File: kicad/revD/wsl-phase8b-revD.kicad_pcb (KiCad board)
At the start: 4 copper layers, 250 x 240 mm, 299 parts, among them J1 J_PI, J10 J_MOTION_M 5.08mm, J11 J_MOTION_M2 5.08mm, J12 J_MOTION_M1 5.08mm, J13 J_LAMP_LED, J14 J_SAFETY, J15 J_SLOW_IN_C, J16 J_EXT_I2C, J2 J_PWR 5V, J3 J_FAST_IN, J4 J_SLOW_IN_A, J5 J_SLOW_IN_B, J6 J_MOTION_S 5.08mm, J7 J_MOTION_T 5.08mm, J8 J_MOTION_SP 5.08mm, J9 J_MOTION_BE 5.08mm, K1 G5LE S, K2 G5LE T, K3 G5LE SP, K4 G5LE BE, K5 G5LE M, K6 G5LE M2, K7 G5LE M1 DNP, Q1 MMBT3904 S, Q10 2N7002 LED L_STRIKE, Q11 2N7002 LED L_FOUL, Q12 AO3400A kick, Q13 AO3400A wdog, Q14 AO3401A rail pass, Q15 MMBT3904 AND ARM, Q16 MMBT3904 AND RP_OK, Q17 2N7002LT1G TAP 555, Q18 2N7002LT1G TAP KICK, Q19 2N7002LT1G TAP ARM, Q2 MMBT3904 T, Q20 2N7002LT1G TAP RPOK, Q3 MMBT3904 SP, Q4 MMBT3904 BE, Q5 MMBT3904 M, Q6 MMBT3904 M2, Q7 MMBT3904 M1, Q8 2N7002 LED L_FIRST, Q9 2N7002 LED L_SECOND, U1 MCP23017 MCP_IN_A, U10 PC817 DIELL_L, U11 PC817 DIELL_R, U12 PC817 GS1, U13 PC817 GS2, U14 PC817 GS3, U15 PC817 GS4, U16 PC817 GS5, U17 PC817 GS6, U18 PC817 GS7, U19 PC817 GS8, U2 MCP23017 MCP_IN_B, U20 PC817 GS9, U21 PC817 GS10, U22 PC817 GP, U23 PC817 OS, U24 PC817 BS, U25 PC817 PBZ, U26 PC817 PBC, U27 PC817 FOUL, U28 PC817 TENTH, U29 PC817 MAN_T, U3 MCP23017 MCP_OUT_A, U30 PC817 MAN_S, U31 PC817 MAN_SWS, U32 PC817 MAN_SWSR, U33 PC817 AUX1, U34 PC817 AUX2, U35 PC817 AUX3, U36 PC817 AUX4, U37 PC817 AUX5, U38 PC817 AUX6, U39 PC817 AUX7, U4 PC817 SA, U40 PC817 AUX8, U41 PC817 AUX9, U42 PC817 AUX10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

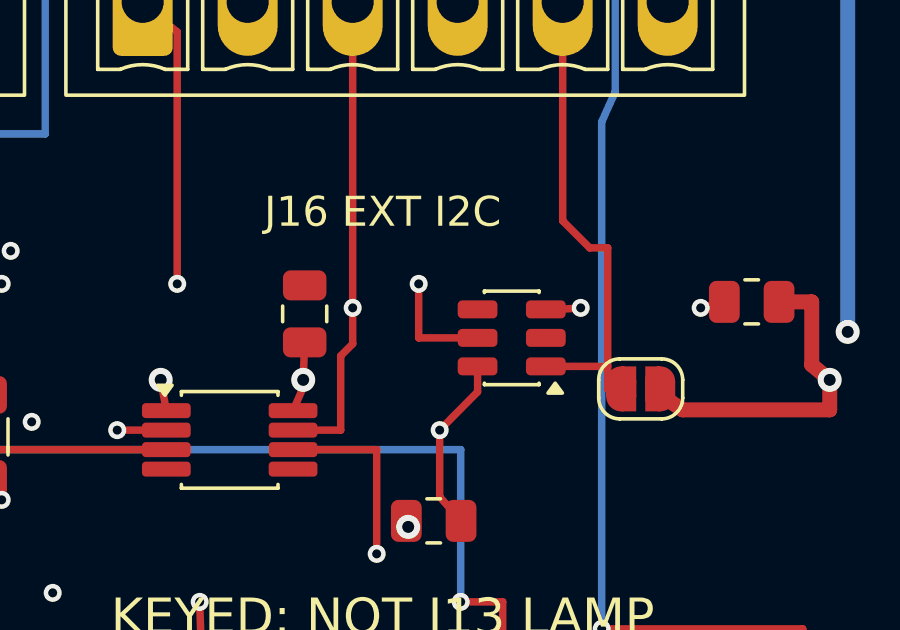
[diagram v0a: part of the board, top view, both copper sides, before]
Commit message: Round-3 fix batch: Codex re-review of the round-2 package — 8 findings, all fixed; full gate chain re-proven
Finding 1 (CRITICAL, fw): v1.2.2 boot-order regression — tap_assert_input_only()
ran before init_inputs(), so every boot latched a spurious tap_dir/SA fault
(GP6-13 still at reset FUNCSEL) and refused RP_OK. Fixed with an inputs_inited
gate (rev_id_inited pattern) + a second invariant pass right after init_inputs().
New test_v12 section R replicates main()'s LITERAL boot order on reset-state pins.

Finding 2 (MAJOR, board): unfused rail sneak path — SRV05-4 VP rode the FUSED
J16_5V node; with JP1 bridged, a J16 5V-to-GND short pulled continuous VCC_3V3
current through IO1's pulse-rated steering diode, defeating the polyfuse. VP now
rides VCC_5V UPSTREAM of F1; the fused pin keeps ESD via the ex-spare IO3
channel (U47.4). Generator/router/audits updated; 271/223 unchanged;
Safety_Rail 13; router self-check 0 (2167 actions); DRC 0/0/0
(DRC-revD-round3-r1.rpt, first pass); board audit ALL PASS (new fail-closed
U47.5-on-VCC_5V assert); diff vs rev-C CLEAN; isolation minima unchanged
2.650/3.350. WVR-ERC-1 waiver now matches the GND/AGND pin pair
order-insensitively (GND pin-order flip from U47.4 leaving GND) — stricter:
both pins must be named.

Finding 3 (MAJOR, Pi): fw_identity chain dead-ended — the typed record was
drained and discarded, and nothing ever sent ID. rp2040_link.start() now sends
ID (request_identity()); _consume_link_records gained the fw_identity branch:
fi1_image and pcb_rev_mismatch are FAULT severity (declared revC expects
strap-read "unknown"). +4 daemon tests, +2 link tests.

Finding 4 (minor, docs): FI-1 BOOTSEL gate vs the bootrom — a plain power cycle
with the jumper held enters the ROM bootloader and can never satisfy the gate.
Working sequences (hold-through-flash / jumper + picotool reboot) documented in
README.md and first-article FA-7 step 0.

Finding 5 (minor, fw): 16-bit epoch aliasing — after 65536 ring-adopting
reboots a stale 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
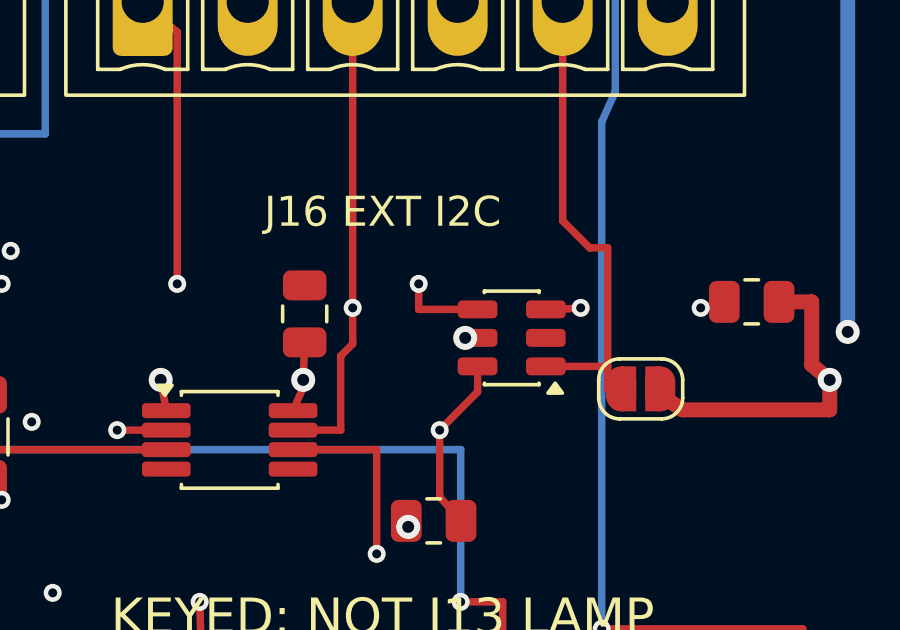
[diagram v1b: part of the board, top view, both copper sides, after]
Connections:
- U47 pad 4: GND -> J16_5V
- U47 pad 5: J16_5V -> VCC_5V
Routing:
- net J16_5V: track 35.8 -> 34.8 mm
- net VCC_5V: track 534.5 -> 535.1 mm, vias 18 -> 19

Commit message: Round-4 board (Codex 'Rev-D r5' + Claude F4 fix): 47k PC817 collector pull-ups, fab r4 tombstoned, r5 release package
Coordinated value-only change: SKiDL generator Rpu_* 10k -> 47k with rationale,
netlist + kicad_pcb exactly 40 Value-field swaps, ZERO copper/geometry/net changes
(frozen-copper rule respected). Fab r4 captured the 47k change but predates the
runtime-bias gate -> tombstoned; r5 is the orderable package (manifest 45/45,
DRC 0/0/0 in reports/).

Claude audit 2026-07-24: full gate chain independently re-run - generator ERC
waiver PASS, netlist reproduced BYTE-IDENTICAL 1d5d36f2..., revC->revD diff clean
55/39/11, kicad-cli 10.0 DRC 0/0, audit_revD_board ALL PASS (exact R4..R82 47k
set), netclass 103/4/13/82/21 Safety_Rail=13, r5 manifest re-hash 45/45,
first-article map 271 rows/40x47k/28 DNP. F4 fixed: ERC canonicalizer now orders
operands inside conflict lines so regeneration reproduces ERC c5dfdf52...
byte-identically. Electrical merit verified (opto sink 264uA->56uA, VIH margin
0.613V); turn-off edge + transient-immunity risks measurement-gated by revised
FA-9 (both edges <=100us, hot open-node >=2.84V) with fleet NO-GO retained.

Co-Authored-By: Claude Fable 5 <noreply@anthropic.com>
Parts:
- R10, R12, R14, R16, R18, R20, R22, R24, R26, R28, R30, R32, R34, R36, R38, R4, R40, R42, R44, R46, R48, R50, R52, R54, R56, R58, R6, R60, R62, R64, R66, R68, R70, R72, R74, R76, R78, R8, R80, R82: value 10k -> 47k
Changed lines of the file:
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@@
 			)
 		)
-		(property "Value" "10k"
+		(property "Value" "47k"
 			(at 0 1.65 0)
 			(layer "F.Fab")
@@
 			)
 		)
-		(property "Value" "10k"
+		(property "Value" "47k"
 			(at 0 1.65 0)
 			(layer "F.Fab")
@@
 			)
 		)
-		(property "Value" "10k"
+		(property "Value" "47k"
 			(at 0 1.65 0)
 			(layer "F.Fab")
@@
 			)
 		)
-		(property "Value" "10k"
+		(property "Value" "47k"
 			(at 0 1.65 0)
 			(layer "F.Fab")
@@
 			)
 		)
-		(property "Value" "10k"
+		(property "Value" "47k"
 			(at 0 1.65 0)
 			(layer "F.Fab")
@@
 			)
 		)
-		(property "Value" "10k"
+		(property "Value" "47k"
 			(at 0 1.65 0)
 			(layer "F.Fab")
@@
 			)
 		)
-		(property "Value" "10k"
+		(property "Value" "47k"
 			(at 0 1.65 0)
 			(layer "F.Fab")
@@
 			)
 		)
-		(property "Value" "10k"
+		(property "Value" "47k"
 			(at 0 1.65 0)
 			(layer "F.Fab")
@@
 			)
 		)
-		(property "Value" "10k"
+		(property "Value" "47k"
 			(at 0 1.65 0)
 			(layer "F.Fab")
@@
 			)
 		)
-		(property "Value" "10k"
+		(property "Value" "47k"
 			(at 0 1.65 0)
 			(layer "F.Fab")
@@
 			)
 		)
-		(property "Value" "10k"
+		(property "Value" "47k"
 			(at 0 1.65 0)
 			(layer "F.Fab")
@@
 			)
 		)
-		(property "Value" "10k"
+		(property "Value" "47k"
 			(at 0 1.65 0)
 			(layer "F.Fab")
@@
 			)
 		)
-		(property "Value" "10k"
+		(property "Value" "47k"
 			(at 0 1.65 0)
 			(layer "F.Fab")
@@
 			)
 		)
-		(property "Value" "10k"
+		(property "Value" "47k"
 			(at 0 1.65 0)
 			(layer "F.Fab")
@@
 			)
 		)
-		(property "Value" "10k"
+		(property "Value" "47k"
 			(at 0 1.65 0)
 			(layer "F.Fab")
@@
 			)
 		)
-		(property "Value" "10k"
+		(property "Value" "47k"
 			(at 0 1.65 0)
 			(layer "F.Fab")
@@
 			)
 		)
-		(property "Value" "10k"
+		(property "Value" "47k"
 			(at 0 1.65 0)
 			(layer "F.Fab")
@@
 			)
 		)
-		(property "Value" "10k"
+		(property "Value" "47k"
 			(at 0 1.65 0)
 			(layer "F.Fab")
@@
 			)
 		)
-		(property "Value" "10k"
+		(property "Value" "47k"
 			(at 0 1.65 0)
 			(layer "F.Fab")
@@
 			)
 		)
-		(property "Value" "10k"
+		(property "Value" "47k"
 			(at 0 1.65 0)
 			(layer "F.Fab")
@@
 			)
 		)
-		(property "Value" "10k"
+		(property "Value" "47k"
 			(at 0 1.65 0)
 			(layer "F.Fab")
@@
 			)
 		)
-		(property "Value" "10k"
+		(property "Value" "47k"
 			(at 0 1.65 0)
 			(layer "F.Fab")
@@
 			)
 		)
-		(property "Value" "10k"
+		(property "Value" "47k"
 			(at 0 1.65 0)
 			(layer "F.Fab")
@@
 			)
 		)
-		(property "Value" "10k"
+		(property "Value" "47k"
 			(at 0 1.65 0)
 			(layer "F.Fab")
@@
 			)
 		)
-		(property "Value" "10k"
+		(property "Value" "47k"
 			(at 0 1.65 0)
 			(layer "F.Fab")
@@
 			)
 		)
-		(property "Value" "10k"
+		(property "Value" "47k"
 			(at 0 1.65 0)
 			(layer "F.Fab")
@@
 			)
 		)
-		(property "Value" "10k"
+		(property "Value" "47k"
 			(at 0 1.65 0)
 			(layer "F.Fab")
@@
 			)
 		)
-		(property "Value" "10k"
+		(property "Value" "47k"
 			(at 0 1.65 0)
 			(layer "F.Fab")
@@
 			)
 		)
-		(property "Value" "10k"
+		(property "Value" "47k"
 			(at 0 1.65 0)
 			(layer "F.Fab")
@@
 			)
 		)
-		(property "Value" "10k"
+		(property "Value" "47k"
 			(at 0 1.65 0)
 			(layer "F.Fab")
@@
 			)
 		)
-		(property "Value" "10k"
+		(property "Value" "47k"
 			(at 0 1.65 0)
 			(layer "F.Fab")
@@
 			)
 		)
-		(property "Value" "10k"
+		(property "Value" "47k"
 			(at 0 1.65 0)
 			(layer "F.Fab")
@@
 			)
 		)
-		(property "Value" "10k"
+		(property "Value" "47k"
 			(at 0 1.65 0)
 			(layer "F.Fab")
@@
 			)
 		)
-		(property "Value" "10k"
+		(property "Value" "47k"
 			(at 0 1.65 0)
 			(layer "F.Fab")
@@
 			)
 		)
-		(property "Value" "10k"
+		(property "Value" "47k"
 			(at 0 1.65 0)
 			(layer "F.Fab")
@@
 			)
 		)
-		(property "Value" "10k"
+		(property "Value" "47k"
 			(at 0 1.65 0)
 			(layer "F.Fab")
@@
 			)
 		)
-		(property "Value" "10k"
+		(property "Value" "47k"
 			(at 0 1.65 0)
 			(layer "F.Fab")
@@
 			)
 		)
-		(property "Value" "10k"
+		(property "Value" "47k"
 			(at 0 1.65 0)
 			(layer "F.Fab")
@@
 			)
 		)
-		(property "Value" "10k"
+		(property "Value" "47k"
 			(at 0 1.65 0)
 			(layer "F.Fab")
@@
 			)
 		)
-		(property "Value" "10k"
+		(property "Value" "47k"
 			(at 0 1.65 0)
 			(layer "F.Fab")

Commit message: rev-D r6: per-channel input protection on all 40 opto channels + review batch
Dylan reopened copper 2026-07-25 so the first article is fleet-intent rather
than frozen-and-bodged. Board revision stays D (never fabricated); this is fab
iteration r6. Firmware NOT touched, NOT flashed.

COPPER (all 40 channels, uniform - no per-channel stuffing decision):
  FIELD_WET_V -[Rin 2k2]- FIELD_RIN_<n> -[Dser 1N4148WS]- FIELD_LED_<n>
  -[PC817 LED]- FIELD_<n>, with Dclamp_<n> (1N4148WS) anti-parallel across the
  LED and Cflt_<n> (0805, DNP) on the logic side.
  Dser_*/Dclamp_* = D18-D97, POPULATED. Cflt_* = C17-C56, DNP.

Only series-block + clamp TOGETHER close the case: a clamp alone backfeeds Rin
into the shared FIELD_WET_V rail (Vw pulled to 10.8 V at 9.79 mA on PBZ); a
series diode alone leaves LED reverse set by a leakage divider rather than by
construction. The series position is never DNP-empty - that would open-circuit
the channel.

Counts: parts 271->391, nets 223->263, Field_Sense 82->122, DNP 28->68,
placed 243->323, JLC-placed 226->306. Safety_Rail EXACTLY 13 - unchanged.
EXPECTED_JLC_LINES stays 27: the 80 diodes join the existing 1N4148WS line
(qty 8 -> 88), so zero new JLC-assembled part classes.

FR reviews (P1 scripture, in the run log): FR-16 1N4148WS/SOD-323 PASS with an
explicit polarity proof (symbol pin 1 = K, F.Fab cathode bar toward pad 1,
package band at cathode - three independent confirmations); FR-17 2.2uF X7R
0805 PASS (DNP); FR-18 10nF X7R 0805 PASS (DNP, already a locked part).

REVIEW BATCH - 15 findings verified, 14 real and fixed, 1 rejected:
- Spec D.5 claimed a 1.06 mm / 1.77x clearance minimum. Bracketed with
  kicad-cli: 0.90 -> 0 violations, 0.95 -> 117 ("actual 0.9100 mm"), 1.00 -> 148.
  TRUE MINIMUM 0.910 mm = 1.52x, and the binding pair is an r6 clamp pad vs the
  next row's FIELD_LED track, not the track-to-track pair analysed. Gate still
  0/0/0. Corrected in the spec and the .kicad_dru.
- Spec J5/I.2 demanded "sole CHANGED_PART = 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
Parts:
- added C17: 10nF X7R DNP, Capacitor_SMD:C_0805_2012Metric, F.Cu at (86.0, 17.6)
- added C18: 10nF X7R DNP, Capacitor_SMD:C_0805_2012Metric, F.Cu at (86.0, 23.3)
- added C19: 10nF X7R DNP, Capacitor_SMD:C_0805_2012Metric, F.Cu at (86.0, 29.0)
- added C20: 10nF X7R DNP, Capacitor_SMD:C_0805_2012Metric, F.Cu at (86.0, 34.7)
- added C21: 10nF X7R DNP, Capacitor_SMD:C_0805_2012Metric, F.Cu at (86.0, 40.4)
- added C22: 10nF X7R DNP, Capacitor_SMD:C_0805_2012Metric, F.Cu at (86.0, 46.1)
- added C23: 10nF X7R DNP, Capacitor_SMD:C_0805_2012Metric, F.Cu at (86.0, 51.8)
- added C24: 10nF X7R DNP, Capacitor_SMD:C_0805_2012Metric, F.Cu at (86.0, 57.5)
- added C25: 2.2uF X7R DNP, Capacitor_SMD:C_0805_2012Metric, F.Cu at (86.0, 63.2)
- added C26: 2.2uF X7R DNP, Capacitor_SMD:C_0805_2012Metric, F.Cu at (86.0, 68.9)
- added C27: 2.2uF X7R DNP, Capacitor_SMD:C_0805_2012Metric, F.Cu at (86.0, 74.6)
- added C28: 2.2uF X7R DNP, Capacitor_SMD:C_0805_2012Metric, F.Cu at (86.0, 80.3)
- added C29: 2.2uF X7R DNP, Capacitor_SMD:C_0805_2012Metric, F.Cu at (86.0, 86.0)
- added C30: 2.2uF X7R DNP, Capacitor_SMD:C_0805_2012Metric, F.Cu at (86.0, 91.7)
- added C31: 2.2uF X7R DNP, Capacitor_SMD:C_0805_2012Metric, F.Cu at (86.0, 97.4)
- added C32: 2.2uF X7R DNP, Capacitor_SMD:C_0805_2012Metric, F.Cu at (86.0, 103.1)
- added C33: 2.2uF X7R DNP, Capacitor_SMD:C_0805_2012Metric, F.Cu at (86.0, 108.8)
- added C34: 2.2uF X7R DNP, Capacitor_SMD:C_0805_2012Metric, F.Cu at (86.0, 114.5)
- added C35: 2.2uF X7R DNP, Capacitor_SMD:C_0805_2012Metric, F.Cu at (86.0, 120.2)
- added C36: 2.2uF X7R DNP, Capacitor_SMD:C_0805_2012Metric, F.Cu at (86.0, 125.9)
- added C37: 2.2uF X7R DNP, Capacitor_SMD:C_0805_2012Metric, F.Cu at (86.0, 131.6)
- added C38: 2.2uF X7R DNP, Capacitor_SMD:C_0805_2012Metric, F.Cu at (86.0, 137.3)
- added C39: 2.2uF X7R DNP, Capacitor_SMD:C_0805_2012Metric, F.Cu at (86.0, 143.0)
- added C40: 2.2uF X7R DNP, Capacitor_SMD:C_0805_2012Metric, F.Cu at (86.0, 148.7)
- added C41: 2.2uF X7R DNP, Capacitor_SMD:C_0805_2012Metric, F.Cu at (86.0, 154.4)
- added C42: 2.2uF X7R DNP, Capacitor_SMD:C_0805_2012Metric, F.Cu at (86.0, 160.1)
- added C43: 2.2uF X7R DNP, Capacitor_SMD:C_0805_2012Metric, F.Cu at (86.0, 165.8)
- added C44: 2.2uF X7R DNP, Capacitor_SMD:C_0805_2012Metric, F.Cu at (86.0, 171.5)
- added C45: 2.2uF X7R DNP, Capacitor_SMD:C_0805_2012Metric, F.Cu at (86.0, 177.2)
- added C46: 2.2uF X7R DNP, Capacitor_SMD:C_0805_2012Metric, F.Cu at (86.0, 182.9)
- added C47: 2.2uF X7R DNP, Capacitor_SMD:C_0805_2012Metric, F.Cu at (86.0, 188.6)
- added C48: 2.2uF X7R DNP, Capacitor_SMD:C_0805_2012Metric, F.Cu at (86.0, 194.3)
- added C49: 2.2uF X7R DNP, Capacitor_SMD:C_0805_2012Metric, F.Cu at (86.0, 200.0)
- added C50: 2.2uF X7R DNP, Capacitor_SMD:C_0805_2012Metric, F.Cu at (86.0, 205.7)
- added C51: 2.2uF X7R DNP, Capacitor_SMD:C_0805_2012Metric, F.Cu at (86.0, 211.4)
- added C52: 2.2uF X7R DNP, Capacitor_SMD:C_0805_2012Metric, F.Cu at (86.0, 217.1)
- added C53: 2.2uF X7R DNP, Capacitor_SMD:C_0805_2012Metric, F.Cu at (86.0, 222.8)
- added C54: 2.2uF X7R DNP, Capacitor_SMD:C_0805_2012Metric, F.Cu at (86.0, 228.5)
- added C55: 2.2uF X7R DNP, Capacitor_SMD:C_0805_2012Metric, F.Cu at (86.0, 234.2)
- added C56: 2.2uF X7R DNP, Capacitor_SMD:C_0805_2012Metric, F.Cu at (90.0, 237.1)
- added D18: 1N4148, Diode_SMD:D_SOD-323, F.Cu at (62.0, 11.2)
- added D19: 1N4148, Diode_SMD:D_SOD-323, F.Cu at (70.0, 14.5)
- added D20: 1N4148, Diode_SMD:D_SOD-323, F.Cu at (62.0, 19.9)
- added D21: 1N4148, Diode_SMD:D_SOD-323, F.Cu at (70.0, 20.2)
- added D22: 1N4148, Diode_SMD:D_SOD-323, F.Cu at (62.0, 22.6)
- added D23: 1N4148, Diode_SMD:D_SOD-323, F.Cu at (70.0, 25.9)
- added D24: 1N4148, Diode_SMD:D_SOD-323, F.Cu at (62.0, 28.3)
- added D25: 1N4148, Diode_SMD:D_SOD-323, F.Cu at (70.0, 31.6)
- added D26: 1N4148, Diode_SMD:D_SOD-323, F.Cu at (62.0, 34.0)
- added D27: 1N4148, Diode_SMD:D_SOD-323, F.Cu at (70.0, 37.3)
- added D28: 1N4148, Diode_SMD:D_SOD-323, F.Cu at (62.0, 39.7)
- added D29: 1N4148, Diode_SMD:D_SOD-323, F.Cu at (70.0, 43.0)
- added D30: 1N4148, Diode_SMD:D_SOD-323, F.Cu at (62.0, 45.4)
- added D31: 1N4148, Diode_SMD:D_SOD-323, F.Cu at (70.0, 48.7)
- added D32: 1N4148, Diode_SMD:D_SOD-323, F.Cu at (62.0, 51.1)
- added D33: 1N4148, Diode_SMD:D_SOD-323, F.Cu at (70.0, 54.4)
- added D34: 1N4148, Diode_SMD:D_SOD-323, F.Cu at (62.0, 56.8)
- added D35: 1N4148, Diode_SMD:D_SOD-323, F.Cu at (70.0, 60.1)
- added D36: 1N4148, Diode_SMD:D_SOD-323, F.Cu at (62.0, 62.5)
- added D37: 1N4148, Diode_SMD:D_SOD-323, F.Cu at (70.0, 65.8)
- added D38: 1N4148, Diode_SMD:D_SOD-323, F.Cu at (62.0, 68.2)
- added D39: 1N4148, Diode_SMD:D_SOD-323, F.Cu at (70.0, 71.5)
- added D40: 1N4148, Diode_SMD:D_SOD-323, F.Cu at (62.0, 73.9)
- added D41: 1N4148, Diode_SMD:D_SOD-323, F.Cu at (70.0, 77.2)
- added D42: 1N4148, Diode_SMD:D_SOD-323, F.Cu at (62.0, 79.6)
- added D43: 1N4148, Diode_SMD:D_SOD-323, F.Cu at (70.0, 82.9)
- added D44: 1N4148, Diode_SMD:D_SOD-323, F.Cu at (62.0, 85.3)
- added D45: 1N4148, Diode_SMD:D_SOD-323, F.Cu at (70.0, 88.6)
- added D46: 1N4148, Diode_SMD:D_SOD-323, F.Cu at (62.0, 91.0)
- added D47: 1N4148, Diode_SMD:D_SOD-323, F.Cu at (70.0, 94.3)
- added D48: 1N4148, Diode_SMD:D_SOD-323, F.Cu at (62.0, 96.7)
- added D49: 1N4148, Diode_SMD:D_SOD-323, F.Cu at (70.0, 100.0)
- added D50: 1N4148, Diode_SMD:D_SOD-323, F.Cu at (62.0, 102.4)
- added D51: 1N4148, Diode_SMD:D_SOD-323, F.Cu at (70.0, 105.7)
- added D52: 1N4148, Diode_SMD:D_SOD-323, F.Cu at (62.0, 108.1)
- added D53: 1N4148, Diode_SMD:D_SOD-323, F.Cu at (70.0, 111.4)
- added D54: 1N4148, Diode_SMD:D_SOD-323, F.Cu at (62.0, 113.8)
- added D55: 1N4148, Diode_SMD:D_SOD-323, F.Cu at (70.0, 117.1)
- added D56: 1N4148, Diode_SMD:D_SOD-323, F.Cu at (62.0, 119.5)
- added D57: 1N4148, Diode_SMD:D_SOD-323, F.Cu at (70.0, 122.8)
- added D58: 1N4148, Diode_SMD:D_SOD-323, F.Cu at (62.0, 125.2)
- added D59: 1N4148, Diode_SMD:D_SOD-323, F.Cu at (70.0, 128.5)
- added D60: 1N4148, Diode_SMD:D_SOD-323, F.Cu at (62.0, 130.9)
- added D61: 1N4148, Diode_SMD:D_SOD-323, F.Cu at (70.0, 134.2)
- added D62: 1N4148, Diode_SMD:D_SOD-323, F.Cu at (62.0, 136.6)
- added D63: 1N4148, Diode_SMD:D_SOD-323, F.Cu at (70.0, 139.9)
- added D64: 1N4148, Diode_SMD:D_SOD-323, F.Cu at (62.0, 142.3)
- added D65: 1N4148, Diode_SMD:D_SOD-323, F.Cu at (70.0, 145.6)
- added D66: 1N4148, Diode_SMD:D_SOD-323, F.Cu at (62.0, 148.0)
- added D67: 1N4148, Diode_SMD:D_SOD-323, F.Cu at (70.0, 151.3)
- added D68: 1N4148, Diode_SMD:D_SOD-323, F.Cu at (62.0, 153.7)
- added D69: 1N4148, Diode_SMD:D_SOD-323, F.Cu at (70.0, 157.0)
- added D70: 1N4148, Diode_SMD:D_SOD-323, F.Cu at (62.0, 159.4)
- added D71: 1N4148, Diode_SMD:D_SOD-323, F.Cu at (70.0, 162.7)
- added D72: 1N4148, Diode_SMD:D_SOD-323, F.Cu at (62.0, 165.1)
- added D73: 1N4148, Diode_SMD:D_SOD-323, F.Cu at (70.0, 168.4)
- added D74: 1N4148, Diode_SMD:D_SOD-323, F.Cu at (62.0, 170.8)
- added D75: 1N4148, Diode_SMD:D_SOD-323, F.Cu at (70.0, 174.1)
- added D76: 1N4148, Diode_SMD:D_SOD-323, F.Cu at (62.0, 176.5)
- added D77: 1N4148, Diode_SMD:D_SOD-323, F.Cu at (70.0, 179.8)
- added D78: 1N4148, Diode_SMD:D_SOD-323, F.Cu at (62.0, 182.2)
- added D79: 1N4148, Diode_SMD:D_SOD-323, F.Cu at (70.0, 185.5)
- added D80: 1N4148, Diode_SMD:D_SOD-323, F.Cu at (62.0, 187.9)
- added D81: 1N4148, Diode_SMD:D_SOD-323, F.Cu at (70.0, 191.2)
- added D82: 1N4148, Diode_SMD:D_SOD-323, F.Cu at (62.0, 193.6)
- added D83: 1N4148, Diode_SMD:D_SOD-323, F.Cu at (70.0, 196.9)
- added D84: 1N4148, Diode_SMD:D_SOD-323, F.Cu at (62.0, 199.3)
- added D85: 1N4148, Diode_SMD:D_SOD-323, F.Cu at (70.0, 202.6)
- added D86: 1N4148, Diode_SMD:D_SOD-323, F.Cu at (62.0, 205.0)
- added D87: 1N4148, Diode_SMD:D_SOD-323, F.Cu at (70.0, 208.3)
- added D88: 1N4148, Diode_SMD:D_SOD-323, F.Cu at (62.0, 210.7)
- added D89: 1N4148, Diode_SMD:D_SOD-323, F.Cu at (70.0, 214.0)
- added D90: 1N4148, Diode_SMD:D_SOD-323, F.Cu at (62.0, 216.4)
- added D91: 1N4148, Diode_SMD:D_SOD-323, F.Cu at (70.0, 219.7)
- added D92: 1N4148, Diode_SMD:D_SOD-323, F.Cu at (62.0, 222.1)
- added D93: 1N4148, Diode_SMD:D_SOD-323, F.Cu at (70.0, 225.4)
- added D94: 1N4148, Diode_SMD:D_SOD-323, F.Cu at (62.0, 227.8)
- added D95: 1N4148, Diode_SMD:D_SOD-323, F.Cu at (70.0, 231.1)
- added D96: 1N4148, Diode_SMD:D_SOD-323, F.Cu at (62.0, 233.5)
- added D97: 1N4148, Diode_SMD:D_SOD-323, F.Cu at (70.0, 236.8)
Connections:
- R11 pad 2: FIELD_LED_TA2 -> FIELD_RIN_TA2
- R13 pad 2: FIELD_LED_TB -> FIELD_RIN_TB
- R15 pad 2: FIELD_LED_DIELL_L -> FIELD_RIN_DIELL_L
- R17 pad 2: FIELD_LED_DIELL_R -> FIELD_RIN_DIELL_R
- R19 pad 2: FIELD_LED_GS1 -> FIELD_RIN_GS1
- R21 pad 2: FIELD_LED_GS2 -> FIELD_RIN_GS2
- R23 pad 2: FIELD_LED_GS3 -> FIELD_RIN_GS3
- R25 pad 2: FIELD_LED_GS4 -> FIELD_RIN_GS4
- R27 pad 2: FIELD_LED_GS5 -> FIELD_RIN_GS5
- R29 pad 2: FIELD_LED_GS6 -> FIELD_RIN_GS6
- R3 pad 2: FIELD_LED_SA -> FIELD_RIN_SA
- R31 pad 2: FIELD_LED_GS7 -> FIELD_RIN_GS7
- R33 pad 2: FIELD_LED_GS8 -> FIELD_RIN_GS8
- R35 pad 2: FIELD_LED_GS9 -> FIELD_RIN_GS9
- R37 pad 2: FIELD_LED_GS10 -> FIELD_RIN_GS10
- R39 pad 2: FIELD_LED_GP -> FIELD_RIN_GP
- R41 pad 2: FIELD_LED_OS -> FIELD_RIN_OS
- R43 pad 2: FIELD_LED_BS -> FIELD_RIN_BS
- R45 pad 2: FIELD_LED_PBZ -> FIELD_RIN_PBZ
- R47 pad 2: FIELD_LED_PBC -> FIELD_RIN_PBC
- R49 pad 2: FIELD_LED_FOUL -> FIELD_RIN_FOUL
- R5 pad 2: FIELD_LED_SB -> FIELD_RIN_SB
- R51 pad 2: FIELD_LED_TENTH -> FIELD_RIN_TENTH
- R53 pad 2: FIELD_LED_MAN_T -> FIELD_RIN_MAN_T
- R55 pad 2: FIELD_LED_MAN_S -> FIELD_RIN_MAN_S
- R57 pad 2: FIELD_LED_MAN_SWS -> FIELD_RIN_MAN_SWS
- R59 pad 2: FIELD_LED_MAN_SWSR -> FIELD_RIN_MAN_SWSR
- R61 pad 2: FIELD_LED_AUX1 -> FIELD_RIN_AUX1
- R63 pad 2: FIELD_LED_AUX2 -> FIELD_RIN_AUX2
- R65 pad 2: FIELD_LED_AUX3 -> FIELD_RIN_AUX3
- R67 pad 2: FIELD_LED_AUX4 -> FIELD_RIN_AUX4
- R69 pad 2: FIELD_LED_AUX5 -> FIELD_RIN_AUX5
- R7 pad 2: FIELD_LED_SC -> FIELD_RIN_SC
- R71 pad 2: FIELD_LED_AUX6 -> FIELD_RIN_AUX6
- R73 pad 2: FIELD_LED_AUX7 -> FIELD_RIN_AUX7
- R75 pad 2: FIELD_LED_AUX8 -> FIELD_RIN_AUX8
- R77 pad 2: FIELD_LED_AUX9 -> FIELD_RIN_AUX9
- R79 pad 2: FIELD_LED_AUX10 -> FIELD_RIN_AUX10
- R81 pad 2: FIELD_LED_AUX11 -> FIELD_RIN_AUX11
- R9 pad 2: FIELD_LED_TA1 -> FIELD_RIN_TA1
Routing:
- net FIELD_RIN_SB: track 0.00 -> 5.09 mm
- net RP2040_OK: track 438.8 -> 433.8 mm
- net FIELD_LED_SB: track 16.9 -> 12.6 mm, vias 2 -> 0
- net FIELD_WET_V: track 373.8 -> 369.8 mm
- net SLOW_AUX11: track 154.4 -> 156.5 mm
- net FIELD_RIN_TENTH: track 0.00 -> 2.04 mm
- net FIELD_RIN_TB: track 0.00 -> 2.04 mm
- net FIELD_RIN_TA2: track 0.00 -> 2.04 mm
- net FIELD_RIN_TA1: track 0.00 -> 2.04 mm
- net FIELD_RIN_SC: track 0.00 -> 2.04 mm
- net FIELD_RIN_SA: track 0.00 -> 2.04 mm
- net FIELD_RIN_PBZ: track 0.00 -> 2.04 mm
- net FIELD_RIN_PBC: track 0.00 -> 2.04 mm
- net FIELD_RIN_OS: track 0.00 -> 2.04 mm
- net FIELD_RIN_MAN_T: track 0.00 -> 2.04 mm
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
